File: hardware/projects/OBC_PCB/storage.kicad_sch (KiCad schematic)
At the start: 8 parts, among them J2 DM3CS-SF

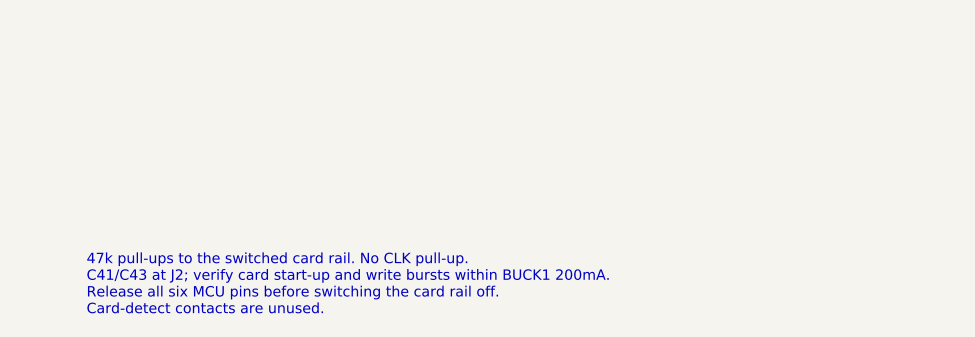
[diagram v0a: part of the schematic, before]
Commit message: hardware: tidy the QFN schematic layout and style
Layout pass on the eight sheets. ERC stays at 0 violations on OBC_PCB and
USB_Baseboard. A netlist comparison shows the same 127 net partitions and
the same components, values and footprints.

Root sheet
- Draw SCL, SDA, COM_EN, LOUD, SHPHLD, BTN_SELECT and BUZZER_PWM as label
  stubs. Wire crossings fall from 38 to 0.
- Redraw the DCC/DECD/DECA/DECRF network as a chain without crossings.
- Move R5 and C26 clear of the crystal wires. Use a ground symbol on Y1
  instead of a label named GND.
- Hang the I2C test points on the U6C stubs.

Power sheet
- Attach the VBUS, VBAT and GND power flags to their nets.
- Tap TP1 onto the SHPHLD wire.
- Use a +3V2 symbol on LSIN2 instead of a label.
- Route SW2, the VSET straps and the CFG resistors without crossings.
- Move the SEL ground away from the LX1 pin.
- Show LSOUT1(GND) and INT(GND) for the unused LS1 and BMP581 pins.

Display, GNSS, user I/O
- Move J1 pin VA below VB so the VCOM/VB link no longer crosses VA.
- Move the GNSS FTE labels clear of the antenna pin 3 wire.
- Straighten the piezo wiring. Put the GND probe pad above its ground
  symbol.

Style
- One heading size (1.8 bold), one sub-heading size (1.27 bold) and one
  note size (1.0).
- Hide the voltage, dielectric and tolerance fields on the GNSS and radio
  sheets. Remove their dashed frames. Move both sheets to the top-left.
- Use Rev QFN and the same title format on every sheet.
- Set TP1 and TP2 to in_bom no like the other probe pads.
- Add C21 to the VDD bypass note.

Net names change for five nets because their labels are now on the root
sheet: BTN_SELECT, BUZZER_PWM, COM_EN, LOUD and SHPHLD. No net class
pattern uses them.

Co-Authored-By: Claude Sonnet 5.5 <noreply@anthropic.com>
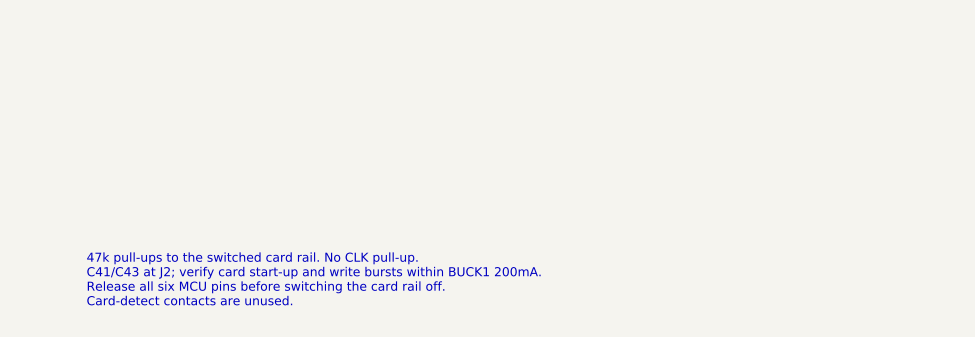
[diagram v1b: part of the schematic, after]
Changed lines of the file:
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@@
 		(effects
 			(font
-				(size 1.15 1.15)
+				(size 1.0 1.0)
 			)
 			(justify left top)

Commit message: hardware: set the SD rail to 3.2 V, fix Y1 and tidy capacitor parts
- Power sheet note: BUCK1 runs at 3.2 V for the SD card, enabled after
  BUCK2 is at 3.2 V. C41 bias note follows. The +3V3_SD net keeps its
  name because the project net classes use it.
- Y1: CX2016DB32000D0FLJCC. It has +/-10 ppm tolerance and +/-15 ppm
  stability, 25 ppm in total against the 40 ppm Bluetooth LE limit in the
  nRF54LM20A HFXO specification. Same 2.0 x 1.6 mm package, 8 pF load.
- C47, C48 and C50 keep the dnp flag. Their value reads "tune (C0G)"
  instead of "DNP", so the BOM keeps the part class.
- C49 uses the same 2.2 uF 16 V X7R 0603 part as C39 and C40.

ERC stays at 0 violations. Only the three capacitor values change in the
netlist.

Co-Authored-By: Claude Sonnet 5.5 <noreply@anthropic.com>
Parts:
- C41: Capacitance at bias Minimum 4.7uF at 3.3V over tolerance and temperature -> Minimum 4.7uF at 3.2V over tolerance and temperature
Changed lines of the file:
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@@
 			)
 		)
-		(property "Capacitance at bias" "Minimum 4.7uF at 3.3V over tolerance and temperature"
+		(property "Capacitance at bias" "Minimum 4.7uF at 3.2V over tolerance and temperature"
 			(at -149.86 -66.04 0)
 			(hide yes)
